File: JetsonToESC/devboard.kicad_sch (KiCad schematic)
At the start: 15 parts, among them U1 ESP32-C3_SUPERMINI_TH, U4 MCP23018x-x-SS, U6 ULN2003

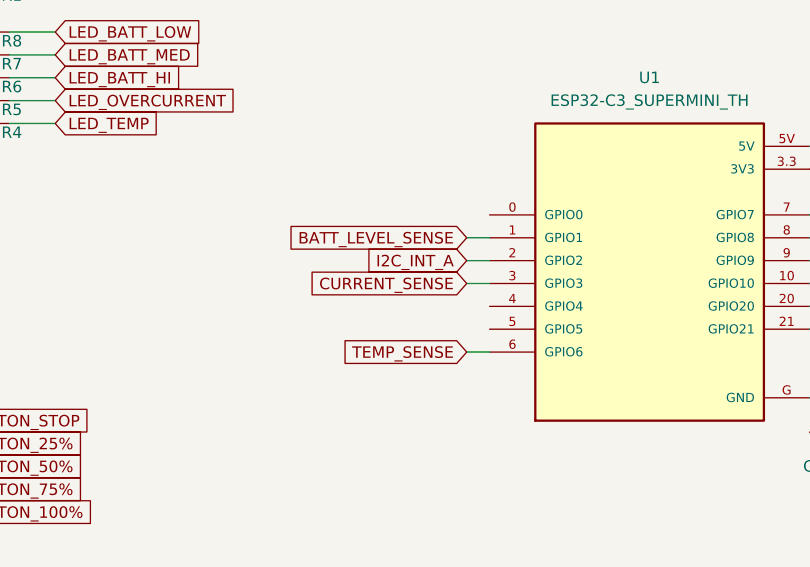
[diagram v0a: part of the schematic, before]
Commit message: Updated connector and temp sensor into IDC and NTC
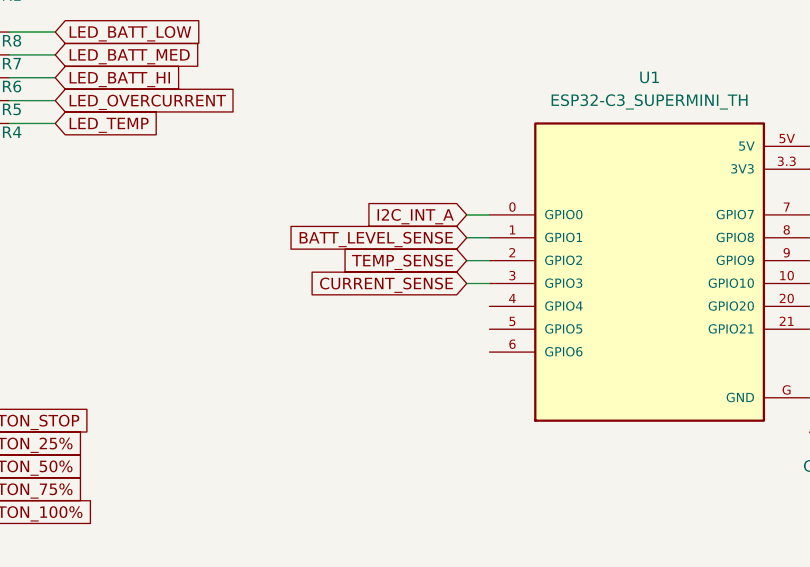
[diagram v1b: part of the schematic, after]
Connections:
- net I2C_INT_A: now also U1.0 (GPIO0); no longer U1.2 (GPIO2)
- net TEMP_SENSE: now also U1.2 (GPIO2); no longer U1.6 (GPIO6)
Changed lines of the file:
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@@
+	(wire
+		(pts
+			(xy 127 58.42) (xy 129.54 58.42)
+		)
+		(stroke
+			(width 0)
+			(type default)
+		)
+	)
 	(wire
 		(pts
@@
 	(wire
 		(pts
-			(xy 127 73.66) (xy 129.54 73.66)
-		)
-		(stroke
-			(width 0)
-			(type default)
-		)
-	)
-	(wire
-		(pts
 			(xy 52.07 71.12) (xy 52.07 73.66)
 		)
@@
 		)
 	)
+	(global_label "PWM"
+		(shape input)
+		(at 39.37 33.02 180)
+		(fields_autoplaced yes)
+		(effects
+			(font
+				(size 1.27 1.27)
+			)
+			(justify right)
+		)
+		(property "Intersheetrefs" "${INTERSHEET_REFS}"
+			(at 32.212 33.02 0)
+			(effects
+				(font
+					(size 1.27 1.27)
+				)
+				(justify right)
+				(hide yes)
+			)
+		)
+	)
+	(global_label "LED_BATT_HI"
+		(shape input)
+		(at 81.28 43.18 0)
+		(fields_autoplaced yes)
+		(effects
+			(font
+				(size 1.27 1.27)
+			)
+			(justify left)
+		)
+		(property "Intersheetrefs" "${INTERSHEET_REFS}"
+			(at 95.8766 43.18 0)
+			(effects
+				(font
+					(size 1.27 1.27)
+				)
+				(justify left)
+				(hide yes)
+			)
+		)
+	)
+	(global_label "BATT_MED"
+		(shape input)
+		(at 71.12 106.68 0)
+		(fields_autoplaced yes)
+		(effects
+			(font
+				(size 1.27 1.27)
+			)
+			(justify left)
+		)
+		(property "Intersheetrefs" "${INTERSHEET_REFS}"
+			(at 83.237 106.68 0)
+			(effects
+				(font
+					(size 1.27 1.27)
+				)
+				(justify left)
+				(hide yes)
+			)
+		)
+	)
+	(global_label "BATT_LOW"
+		(shape input)
+		(at 40.64 45.72 180)
+		(fields_autoplaced yes)
+		(effects
+			(font
+				(size 1.27 1.27)
+			)
+			(justify right)
+		)
+		(property "Intersheetrefs" "${INTERSHEET_REFS}"
+			(at 28.5834 45.72 0)
+			(effects
+				(font
+					(size 1.27 1.27)
+				)
+				(justify right)
+				(hide yes)
+			)
+		)
+	)
+	(global_label "TEMP_SENSE"
+		(shape input)
+		(at 127 63.5 180)
+		(fields_autoplaced yes)
+		(effects
+			(font
+				(size 1.27 1.27)
+			)
+			(justify right)
+		)
+		(property "Intersheetrefs" "${INTERSHEET_REFS}"
+			(at 112.1617 63.5 0)
+			(effects
+				(font
+					(size 1.27 1.27)
+				)
+				(justify right)
+				(hide yes)
+			)
+		)
+	)
 	(global_label "I2C_INT_A"
 		(shape input)
-		(at 127 63.5 180)
+		(at 127 58.42 180)
 		(fields_autoplaced yes)
 		(effects
@@
 		)
 		(property "Intersheetrefs" "${INTERSHEET_REFS}"
-			(at 115.0038 63.5 0)
-			(effects
-				(font
-					(size 1.27 1.27)
-				)
-				(justify right)
-				(hide yes)
-			)
-		)
-	)
-	(global_label "PWM"
-		(shape input)
-		(at 39.37 33.02 180)
-		(fields_autoplaced yes)
-		(effects
-			(font
-				(size 1.27 1.27)
-			)
-			(justify right)
-		)
-		(property "Intersheetrefs" "${INTERSHEET_REFS}"
-			(at 32.212 33.02 0)
-			(effects
-				(font
-					(size 1.27 1.27)
-				)
-				(justify right)
-				(hide yes)
-			)
-		)
-	)
-	(global_label "TEMP_SENSE"
-		(shape input)
-		(at 127 73.66 180)
-		(fields_autoplaced yes)
-		(effects
-			(font
-				(size 1.27 1.27)
-			)
-			(justify right)
-		)
-		(property "Intersheetrefs" "${INTERSHEET_REFS}"
-			(at 112.1617 73.66 0)
-			(effects
-				(font
-					(size 1.27 1.27)
-				)
-				(justify right)
-				(hide yes)
-			)
-		)
-	)
-	(global_label "LED_BATT_HI"
-		(shape input)
-		(at 81.28 43.18 0)
-		(fields_autoplaced yes)
-		(effects
-			(font
-				(size 1.27 1.27)
-			)
-			(justify left)
-		)
-		(property "Intersheetrefs" "${INTERSHEET_REFS}"
-			(at 95.8766 43.18 0)
-			(effects
-				(font
-					(size 1.27 1.27)
-				)
-				(justify left)
-				(hide yes)
-			)
-		)
-	)
-	(global_label "BATT_MED"
-		(shape input)
-		(at 71.12 106.68 0)
-		(fields_autoplaced yes)
-		(effects
-			(font
-				(size 1.27 1.27)
-			)
-			(justify left)
-		)
-		(property "Intersheetrefs" "${INTERSHEET_REFS}"
-			(at 83.237 106.68 0)
-			(effects
-				(font
-					(size 1.27 1.27)
-				)
-				(justify left)
-				(hide yes)
-			)
-		)
-	)
-	(global_label "BATT_LOW"
-		(shape input)
-		(at 40.64 45.72 180)
-		(fields_autoplaced yes)
-		(effects
-			(font
-				(size 1.27 1.27)
-			)
-			(justify right)
-		)
-		(property "Intersheetrefs" "${INTERSHEET_REFS}"
-			(at 28.5834 45.72 0)
-			(effects
-				(font
+			(at 115.0038 58.42 0)
+			(effects
+				(font
